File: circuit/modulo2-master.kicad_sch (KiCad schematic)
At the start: 39 parts, among them J1 CONN_01X03, J2 CONN_01X04, J3 CONN_01X04, J5 HOLE, J7 HOLE, Q1 BC547, Q2 BC557, SW1 SW_SRC, U1 LM358

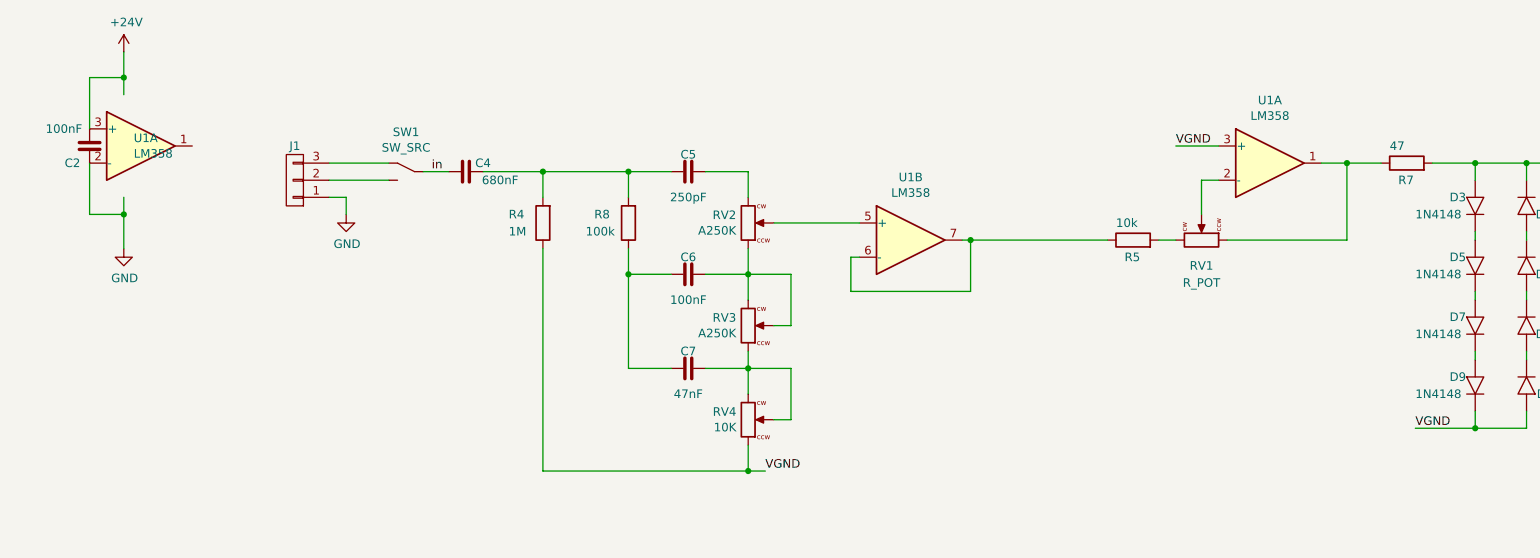
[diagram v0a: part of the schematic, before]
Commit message: added new preamp sim
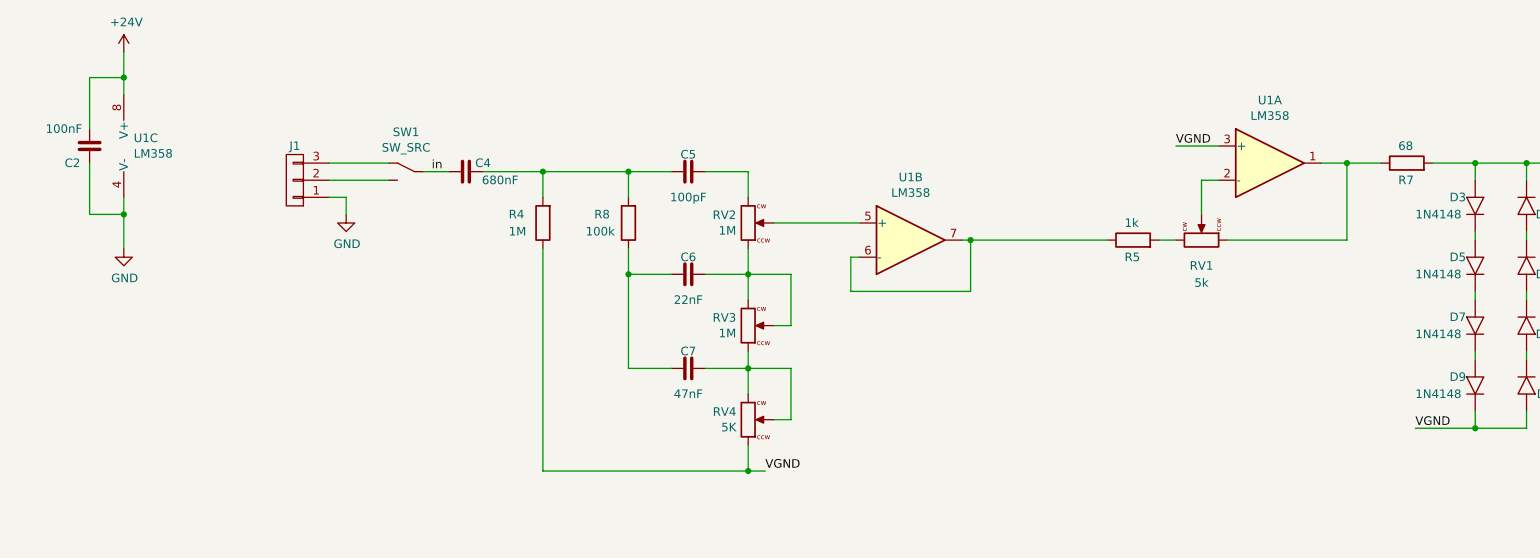
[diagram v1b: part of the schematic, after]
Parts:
- C5: value 250pF -> 100pF
- C6: value 100nF -> 22nF
- R5: value 10k -> 1k
- R7: value 47 -> 68
- RV1: value R_POT -> 5k
- RV2, RV3: value A250K -> 1M
- RV4: value 10K -> 5K
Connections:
- net +24V: now also U1.8 (V+); no longer U1.3 (+)
- net GND: now also U1.4 (V-); no longer U1.2 (-)
